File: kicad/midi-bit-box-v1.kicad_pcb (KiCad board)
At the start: 4 copper layers, 109.2 x 59.1 mm, 60 parts, among them IC1 LM386, IC2 DIP14, K1 TQ2-L-5V, Q1 2N3904, Q2 2N3906, Q3 2N3904, Q4 2N3904, U1 AY-3-8910, U2 L78L09_TO92, U3 NE555P

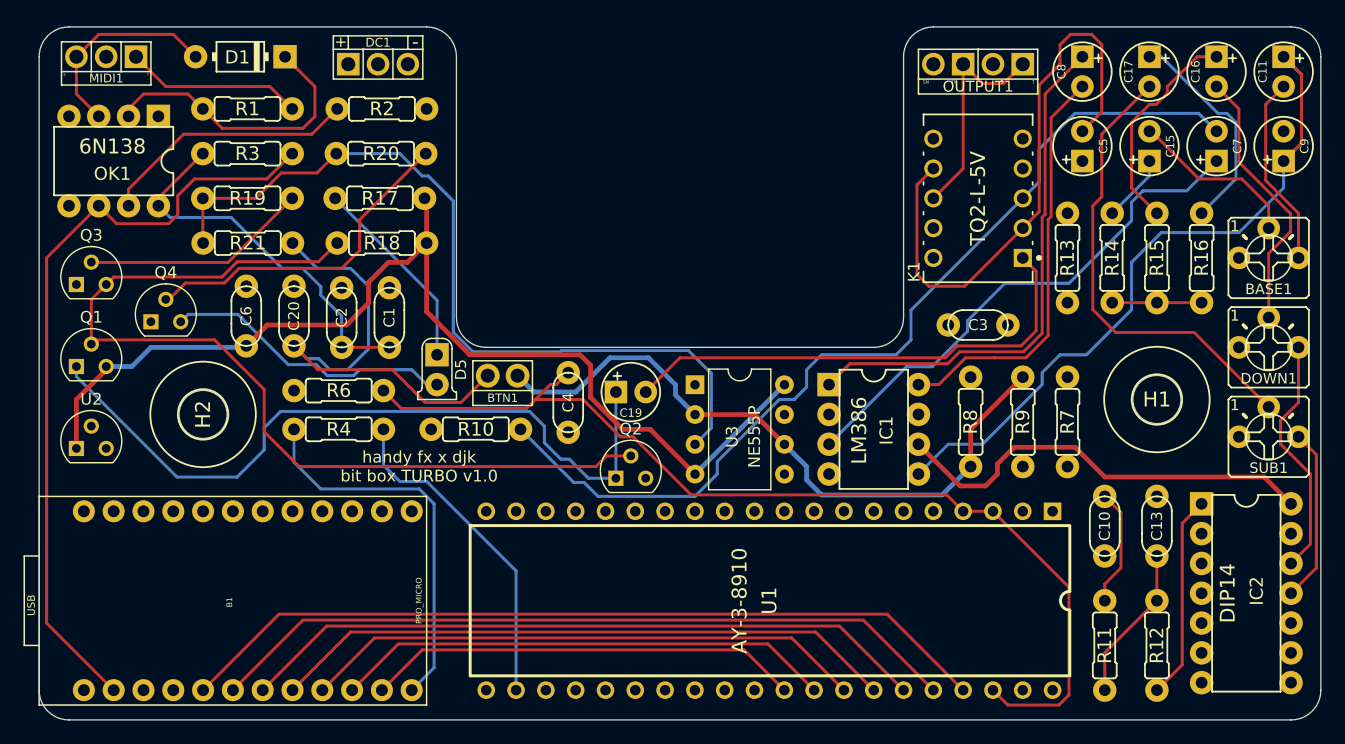
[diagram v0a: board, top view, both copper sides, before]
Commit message: Add files via upload
updated pwr/audio jacks and design rules
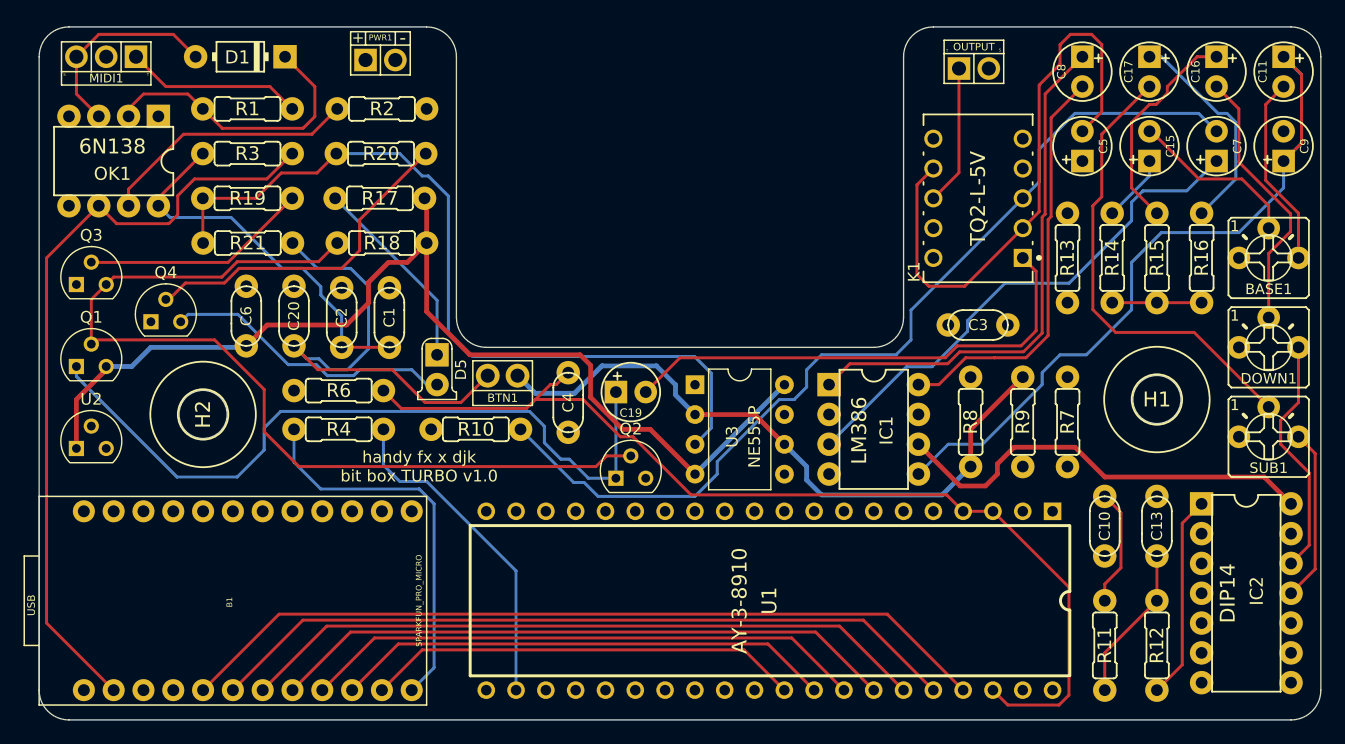
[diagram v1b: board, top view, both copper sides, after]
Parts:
- removed DC1: DC_TRS_PADS, midi-bit-box-v1:DC_TRS
- added PWR1: Jack-DC, midi-bit-box-v1:DC_TS, F.Cu at (130.0, 65.0)
- B1: value PRO_MICRO -> SPARKFUN_PRO_MICRO
- OUTPUT: renamed from OUTPUT1; value SWITCHED_MONO_PADS -> Audio Jack; footprint midi-bit-box-v1:4PADS -> midi-bit-box-v1:2PADS
- Q1, Q2, Q3, Q4, U2: footprint Package_TO_SOT_THT:TO-92 -> midi-bit-box-v1:TO-92-djk-custom
- moved OUTPUT 0.51 mm to (180.6, 65.8), turned to 0 degrees
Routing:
- net Net-(K1-Pad8): track 18.9 -> 12.0 mm
- net GND: track 6.19 -> 0.00 mm
- net VAA: track 172.3 -> 173.7 mm
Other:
- rule pad_to_mask_clearance: 0 -> 0.0508

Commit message: added dual LED
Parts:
- removed D5: LED.2, midi-bit-box-v1:3MM_1
- removed OUTPUT: Audio Jack, midi-bit-box-v1:2PADS
- added D2: LED_Dual_KAK, LED_THT:LED_D5.0mm-3, F.Cu at (133.1, 88.4)
- added OUTPUT1: Audio Jack, midi-bit-box-v1:2PADS, F.Cu at (181.0, 66.1)
- moved C4 1.25 mm to (144.7, 95.5)
- moved R10 1.07 mm to (136.9, 97.6)
- moved R4 1.07 mm to (125.2, 97.6)
- moved R6 1.07 mm to (125.2, 94.3)
- moved BTN1 0.66 mm to (140.9, 92.4)
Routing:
- net Net-(C4-Pad2): track 123.4 -> 121.0 mm
- net Net-(BTN1-Pad2): track 40.7 -> 42.5 mm
- net VDD: track 56.4 -> 54.9 mm
- net Net-(R17-Pad1): track 16.9 -> 18.3 mm
- net Net-(R4-Pad1): track 28.2 -> 27.2 mm
- net Net-(B1-Pad12): track 32.9 -> 31.8 mm
- net Net-(B1-Pad21): track 130.1 -> 131.1 mm

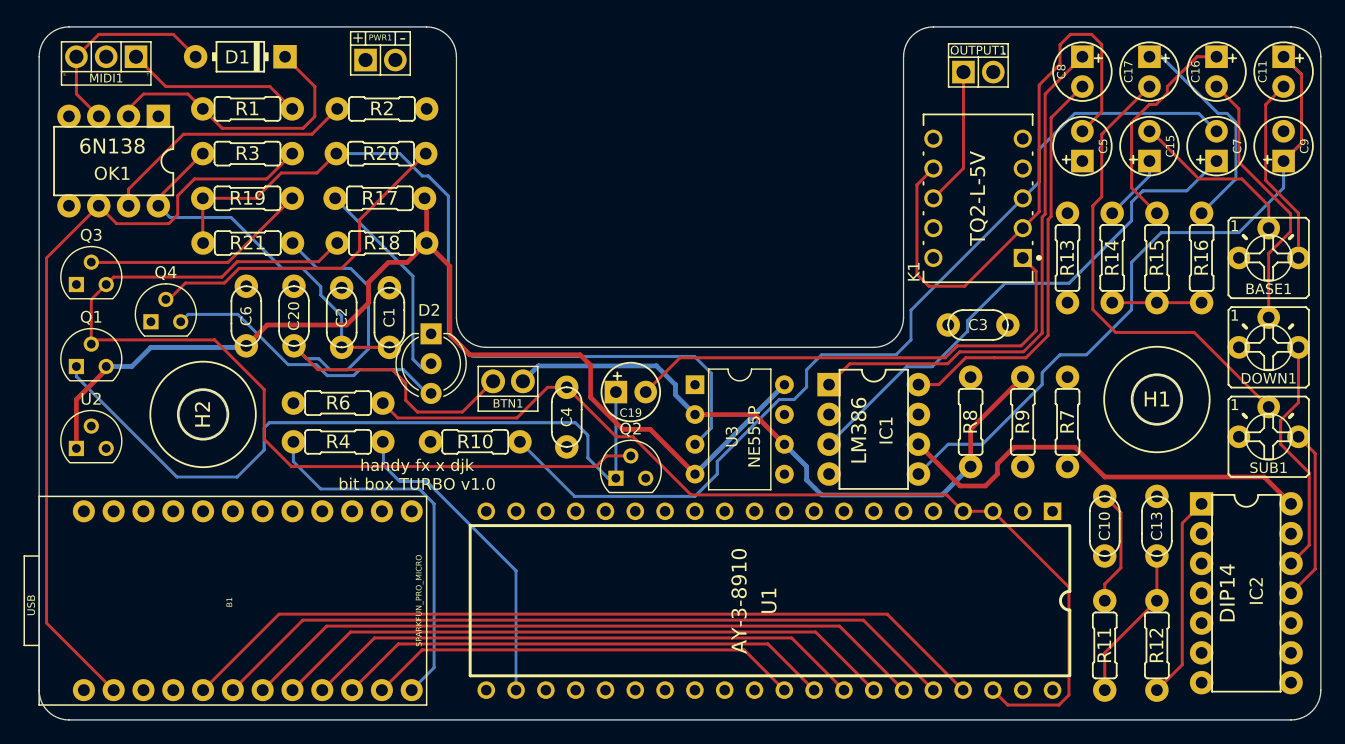
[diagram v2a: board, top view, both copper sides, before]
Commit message: added trimpot to control output volume
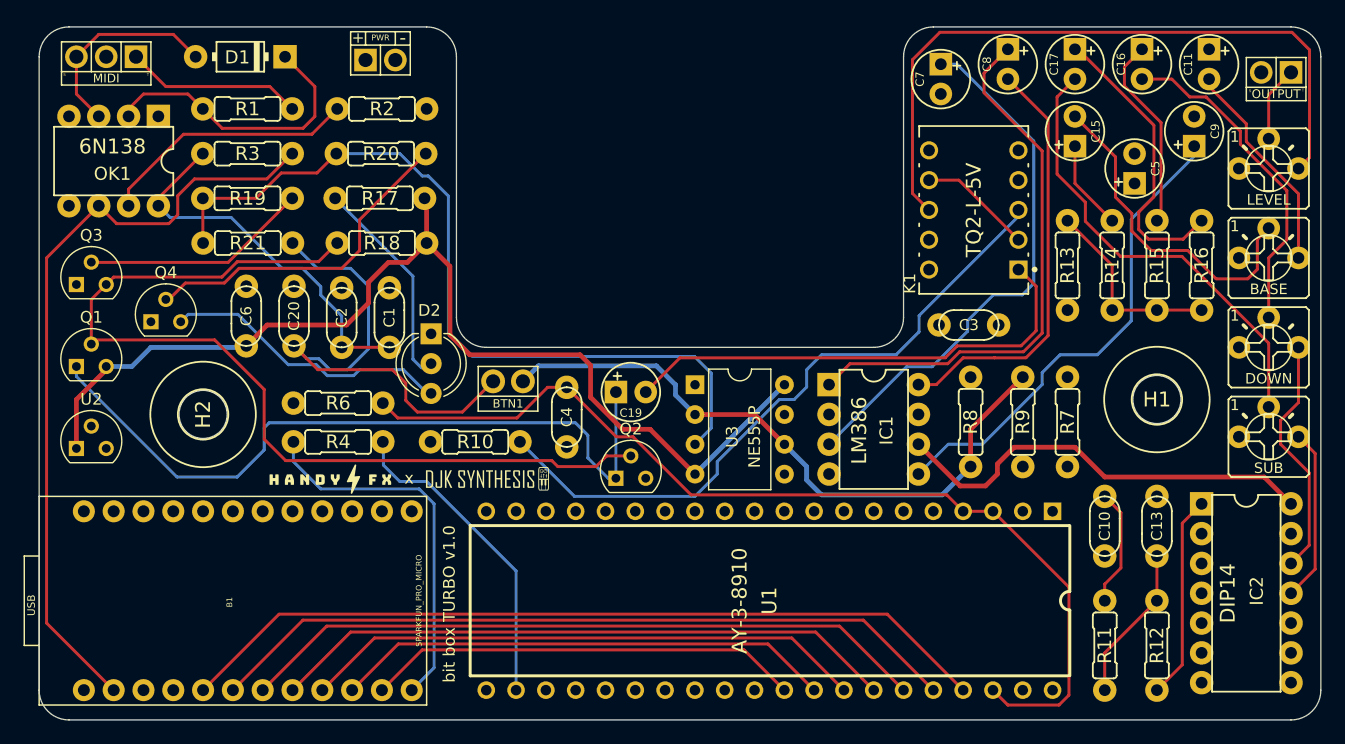
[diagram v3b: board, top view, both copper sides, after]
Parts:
- added G***: LOGO, midi-bit-box-v1:handy-fx-logo, F.Cu at (124.5, 100.8)
- added G***: LOGO, midi-bit-box-v1:djk-synthesis-logo, F.Cu at (137.9, 100.7)
- added LEVEL: 100k, midi-bit-box-v1:TRIM1, F.Cu at (204.5, 74.3)
- moved C7 24.2 mm to (176.5, 66.7), turned to -90 degrees
- moved OUTPUT 22.8 mm to (203.8, 66.1), turned to 180 degrees
- moved C9 7.73 mm to (198.1, 71.1)
- moved C15 6.48 mm to (188.0, 71.1)
- moved C11 6.38 mm to (199.4, 65.4)
- moved C16 6.38 mm to (193.7, 65.4)
- moved C17 6.38 mm to (188.0, 65.4)
- moved C8 6.38 mm to (182.2, 65.4)
- moved C5 4.84 mm to (193.0, 74.3)
- moved K1 1.06 mm to (179.3, 77.8)
- moved C3 0.79 mm to (178.9, 87.6)
- moved R13 0.63 mm to (187.3, 82.5)
- moved R14 0.63 mm to (191.1, 82.5)
- moved R15 0.63 mm to (194.9, 82.5)
- moved R16 0.63 mm to (198.8, 82.5)
- renumbered BASE1 to BASE, DOWN1 to DOWN, MIDI1 to MIDI, OUTPUT1 to OUTPUT, PWR1 to PWR, SUB1 to SUB
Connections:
- OUTPUT pad T: Net-(K1-Pad8) -> Net-(OUTPUT1-PadT)
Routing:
- net Net-(K1-Pad8): track 11.8 -> 59.3 mm
- net Net-(C5-Pad-): track 66.0 -> 38.3 mm
- net Net-(C11-Pad+): track 66.8 -> 51.4 mm
- net Net-(BASE1-Pad2): track 14.7 -> 28.4 mm
- net Net-(C7-Pad-): track 80.0 -> 69.8 mm
- net Net-(R13-Pad2): track 16.8 -> 26.2 mm
- net Net-(C17-Pad+): track 18.6 -> 25.2 mm
- net Net-(OUTPUT1-PadT): track 0.00 -> 6.44 mm
- net Net-(C16-Pad-): track 23.1 -> 28.4 mm
- net Net-(C4-Pad2): track 121.0 -> 117.4 mm
- net Net-(C8-Pad+): track 45.0 -> 47.1 mm
- net Net-(BASE1-Pad3): track 16.4 -> 18.4 mm
- net Net-(C7-Pad+): track 44.5 -> 46.4 mm
- net Net-(C15-Pad+): track 5.76 -> 7.67 mm
- net Net-(C16-Pad+): track 18.5 -> 16.7 mm
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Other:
- board text added: "bit box TURBO v1.0"
- board text added: "x"
- board text removed: "handy fx x djk bit box TURBO v1.0"

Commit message: corrected DC input jack pads
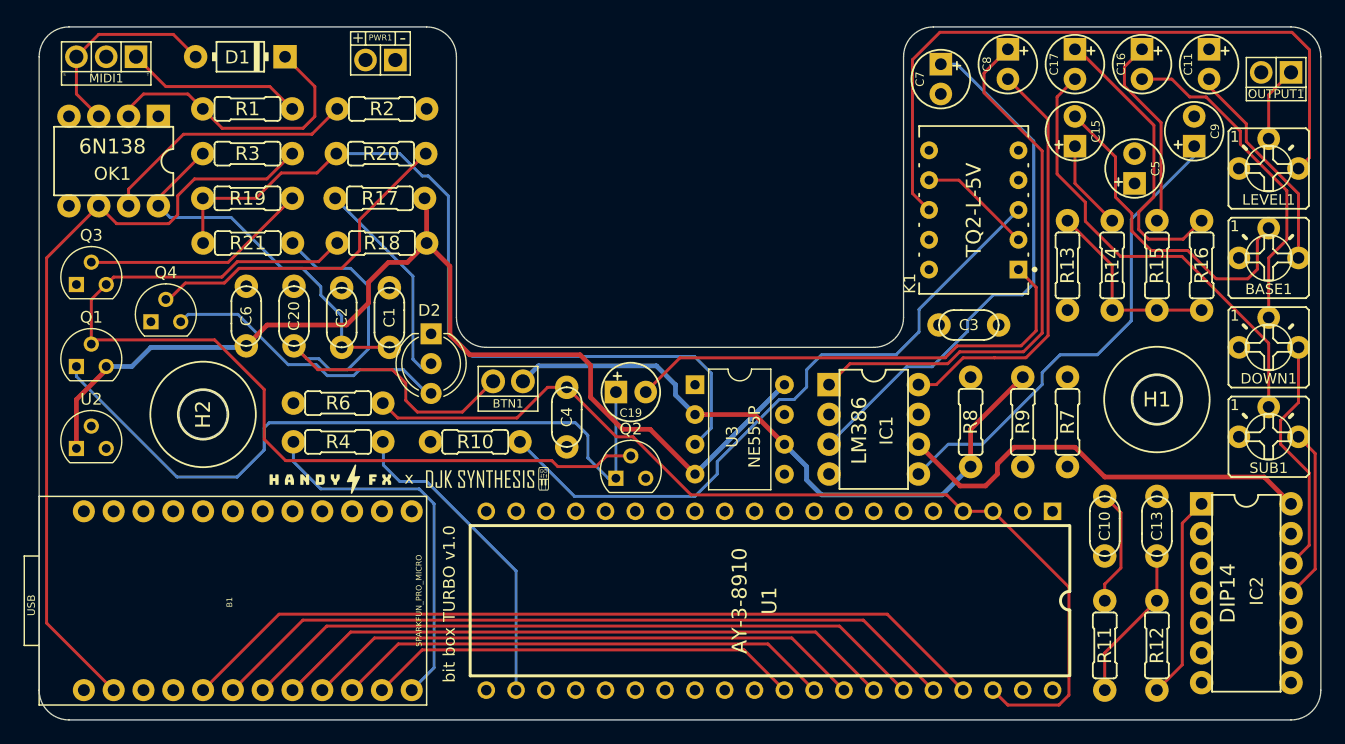
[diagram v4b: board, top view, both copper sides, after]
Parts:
- renumbered BASE to BASE1, DOWN to DOWN1, LEVEL to LEVEL1, MIDI to MIDI1, OUTPUT to OUTPUT1, PWR to PWR1, SUB to SUB1
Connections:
- PWR1 pad 1: GND -> VAA
- PWR1 pad 2: VAA -> GND
